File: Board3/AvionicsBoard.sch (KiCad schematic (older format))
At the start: 58 parts, among them J1 USB_A, J10 I2C, J11 UART, J2 Conn_01x02, J3 SWD, J4 7.2V, J5 3.3V, J6 Micro_SD_Card, J7 RF IN, J8 FDBK, J9 PWM, U1 TL1963, U10 ECS-.327-12.5-17X-TR, U2 ATSAMD21G18, U3 MCP73831, U4 MAX-M8, U5 DS3231-SO16, U6 MPL115A2-LGA, U7 BNO055, U8 RFM95W, U9 ECS-.327-12.5-17X-TR

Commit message: Start general layout
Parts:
- removed J5: 3.3V, Pin_Headers:Pin_Header_Straight_1x02_Pitch2.54mm, symbol Conn_01x02
- added J12: 900MHz_Ant, Pin_Headers:Pin_Header_Straight_1x01_Pitch2.54mm, symbol Conn_01x01
- added J5: SPI, Pin_Headers:Pin_Header_Straight_1x04_Pitch2.54mm, symbol Conn_01x04
- J10, J11: footprint (none) -> Pin_Headers:Pin_Header_Straight_1x03_Pitch2.54mm
- R1, R13, R5, R6: footprint (none) -> Resistors_SMD:R_0603_HandSoldering
- R10, R11, R12, R2, R3, R4, R7, R8, R9: footprint (none) -> Resistors_SMD:R_0805
- U8: footprint (none) -> FoxWestern:RFM95W
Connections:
- net +3V3: now also C15.2, C16.2, R2.1, R3.1, U7.28 (VDDIO), U8.13 (3.3V); no longer BT1.2 (-), C1.2, C10.2, C11.2, C12.2, C13.2, C14.2, C15.1, C16.1, C17.2, C18.1, C19.1, C2.1, C3.1, C4.2, C5.1, C6.2, C7.2, C8.2, C9.2, J1.4 (GND), J1.5 (Shield), J10.3 (Pin_3), J11.3 (Pin_3), J2.1 (Pin_1), J3.4 (Pin_4), J4.2 (Pin_2), J6.6 (VSS), J7.2 (Ext), J8.5 (Pin_5), J8.6 (Pin_6), J9.3 (Pin_3), J9.4 (Pin_4), R12.1, R13.2, R4.1, R6.2, U1.2 (GND), U2.18 (GND), U2.35 (GND), U2.42 (GND), U2.5 (GNDANA), U3.2 (VSS), U4.1 (GND), U4.10 (GND), U4.12 (GND), U5.13 (GND), U6.3 (GND), U7.15 (PIN15), U7.16 (PIN16), U7.18 (COM2), U7.2 (GND), U7.25 (GNDIO), U7.5 (PS1), U7.6 (PS1)
- net CS: now also U8.5 (NSS)
- net MISO: now also U8.2 (MISO), J5.1 (Pin_1)
- net MOSI: now also U8.3 (MOSI), J5.3 (Pin_3)
- net SCK: now also U8.4 (SCK), J5.2 (Pin_2)
- net GND: now reaches U8.1 (GND)
- net GND: now also BT1.2 (-), C1.2, C10.2, C11.2, C12.2, C13.2, C14.2, C15.1, C16.1, C17.2, C18.1, C19.1, C2.1, C3.1, C4.2, C5.1, C6.2, C7.2, C8.2, C9.2, J1.4 (GND), J1.5 (Shield), J10.3 (Pin_3), J11.3 (Pin_3), J2.1 (Pin_1), J3.4 (Pin_4), J4.2 (Pin_2), J6.6 (VSS), J7.2 (Ext), J8.5 (Pin_5), J8.6 (Pin_6), J9.3 (Pin_3), J9.4 (Pin_4), R12.1, R13.2, R4.1, R6.2, U1.2 (GND), U2.18 (GND), U2.35 (GND), U2.42 (GND), U2.5 (GNDANA), U3.2 (VSS), U4.1 (GND), U4.10 (GND), U4.12 (GND), U5.13 (GND), U6.3 (GND), U7.15 (PIN15), U7.16 (PIN16), U7.18 (COM2), U7.2 (GND), U7.25 (GNDIO), U7.5 (PS1), U7.6 (PS1), U8.10 (GND), U8.8 (GND), J5.4 (Pin_4)
- net at U8.9 (ANT): now also J12.1 (Pin_1)
- no-connect marks 33 -> 37
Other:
- moved on the sheet: J1, R5, R6, U8

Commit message: Finished routing board, added logo
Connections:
- net CS: no longer J6.2 (DAT3/CD), U2.23 (PA14)
- net RXD: now also U4.2 (TXD); no longer U4.3 (RXD)
- net TXD: now also U4.3 (RXD); no longer U4.2 (TXD)
- new net D2: J6.2 (DAT3/CD), U2.23 (PA14)
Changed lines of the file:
@@
 	-1   0    0    1
 $EndComp
+Text Label 5950 1100 2    60   ~ 0
+TXD
 Text Label 5950 1000 2    60   ~ 0
-TXD
-Text Label 5950 1100 2    60   ~ 0
 RXD
 $Comp
@@
 	1    0    0    -1
 $EndComp
-Text Label 5650 9000 2    60   ~ 0
-CS
 NoConn ~ 5650 9600
 NoConn ~ 5650 8900

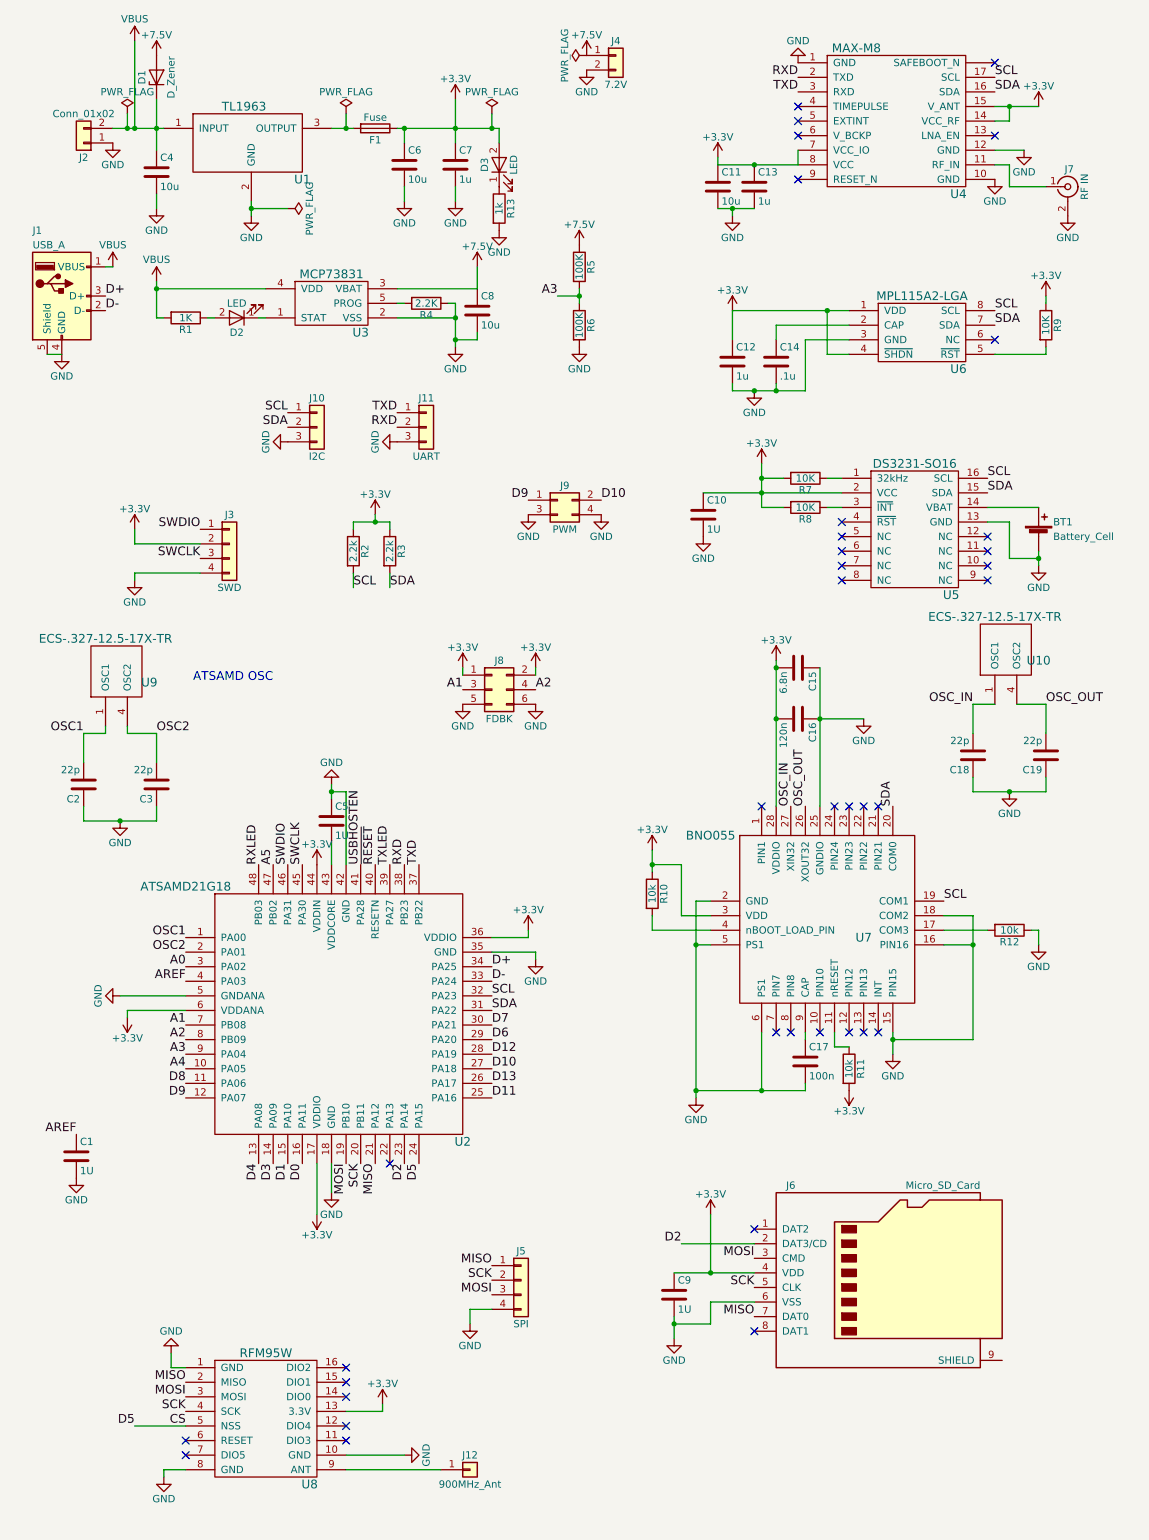
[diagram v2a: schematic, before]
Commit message: Fix BNO055 footprint and board layout
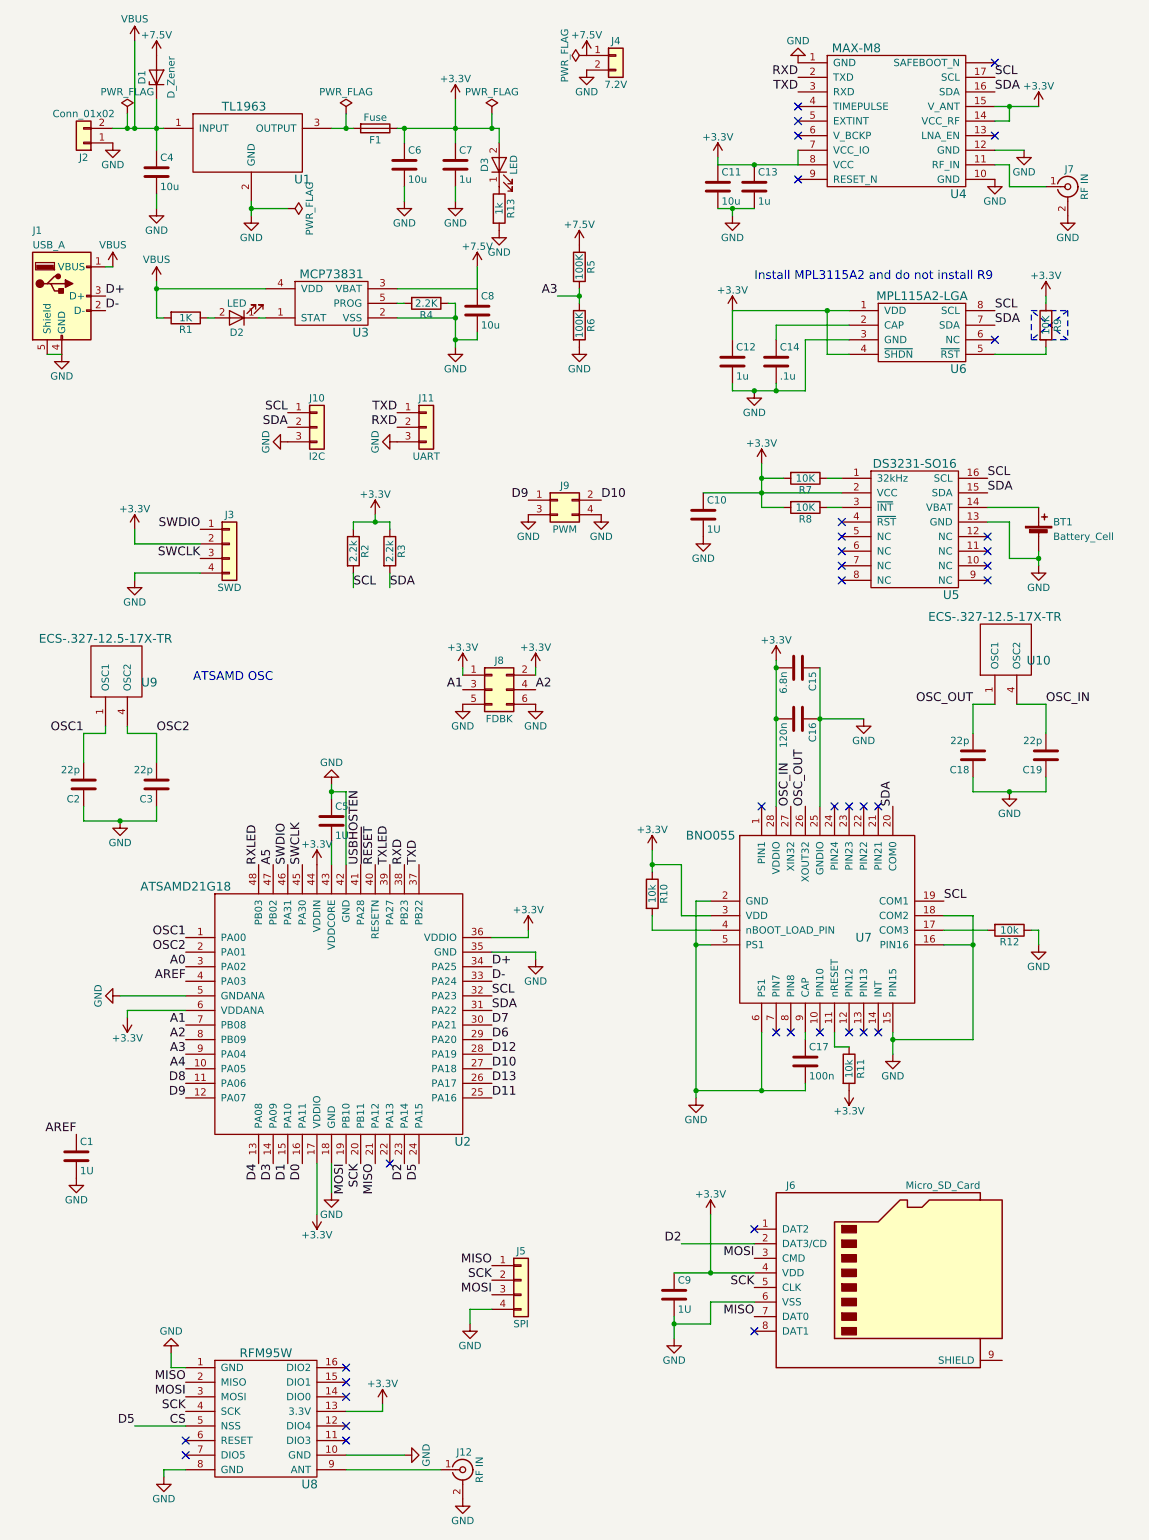
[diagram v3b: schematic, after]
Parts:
- removed J12: 900MHz_Ant, Pin_Headers:Pin_Header_Straight_1x01_Pitch2.54mm, symbol Conn_01x01
- added J12: RF IN, Connectors:SMA_SMD_Jack_Straight, symbol Conn_Coaxial
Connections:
- net GND: now also J12.2 (Ext)
- net OSC_IN: now also C19.2, U10.4 (OSC2); no longer C18.2, U10.1 (OSC1)
- net OSC_OUT: now also C18.2, U10.1 (OSC1); no longer C19.2, U10.4 (OSC2)
- net at U8.9 (ANT): now also J12.1 (In)
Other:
- note added: "Install MPL3115A2 and do not install R9"
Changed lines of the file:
@@
 	-1   0    0    1
 $EndComp
+Text Label 7650 5300 0    60   ~ 0
+OSC_IN
 Text Label 7150 5300 2    60   ~ 0
-OSC_IN
-Text Label 7650 5300 0    60   ~ 0
 OSC_OUT
 $Comp
@@
 Wire Wire Line
 	3250 10450 2850 10450
-$Comp
-L Conn_01x01 J12
-U 1 1 5B2111CE
-P 3700 10550
-F 0 "J12" H 3700 10650 50  0000 C CNN
-F 1 "900MHz_Ant" H 3700 10450 50  0000 C CNN
-F 2 "Pin_Headers:Pin_Header_Straight_1x01_Pitch2.54mm" H 3700 10550 50  0001 C CNN
-F 3 "" H 3700 10550 50  0001 C CNN
-	1    3700 10550
-	1    0    0    -1
-$EndComp
 Wire Wire Line
 	2850 10550 3500 10550
@@
 Wire Wire Line
 	3700 9450 3850 9450
+Wire Notes Line
+	7550 2800 7800 2800
+Wire Notes Line
+	7550 2800 7550 2600
+Wire Notes Line
+	7550 2600 7800 2600
+Wire Notes Line
+	7800 2600 7800 2800
+Wire Notes Line
+	7800 2600 7550 2800
+Wire Notes Line
+	7800 2800 7550 2600
+Text Notes 5650 2400 0    60   ~ 0
+Install MPL3115A2 and do not install R9
+$Comp
+L Conn_Coaxial J12
+U 1 1 5B37DDA7
+P 3650 10550
+F 0 "J12" H 3660 10670 50  0000 C CNN
+F 1 "RF IN" V 3765 10550 50  0000 C CNN
+F 2 "Connectors:SMA_SMD_Jack_Straight" H 3650 10550 50  0001 C CNN
+F 3 "" H 3650 10550 50  0001 C CNN
+	1    3650 10550
+	1    0    0    -1
+$EndComp
+$Comp
+L GND #PWR073
+U 1 1 5B37EDCC
+P 3650 10750
+F 0 "#PWR073" H 3650 10500 50  0001 C CNN
+F 1 "GND" H 3650 10600 50  0000 C CNN
+F 2 "" H 3650 10750 50  0001 C CNN
+F 3 "" H 3650 10750 50  0001 C CNN
+	1    3650 10750
+	1    0    0    -1
+$EndComp
 $EndSCHEMATC
